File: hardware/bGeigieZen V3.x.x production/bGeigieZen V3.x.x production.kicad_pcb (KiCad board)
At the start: 2 copper layers, 129.4 x 64.6 mm, 16 parts, among them J1 M5 2x15 pin, J10 QI GND, J11 QI charger Plus, J2 Geiger IRover, J3 GPS, J4 Geiger Safepulse, J5 Extra support header, J6 Grove, J8 QI charger ground, J9 QI Plus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

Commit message: Fixed some text on V3.0.5 boards
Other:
- board text added: "Grove"
- board text removed: "Groove"
- board text removed: "bGeigieZen V3.0.4 Production"
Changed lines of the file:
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@@
 		)
 	)
-	(gr_text "bGeigieZen\nV3.0.4  Production"
+	(gr_text "bGeigieZen\nV3.0.5  Production"
 		(at 102.7176 83.006 90)
 		(layer "B.SilkS")
@@
 		)
 	)
-	(gr_text "Groove"
+	(gr_text "Grove"
 		(at 163.83 117.6008 90)
 		(layer "F.SilkS")

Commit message: Updated some traces.
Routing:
- net 3.3V: track 117.2 -> 110.8 mm, vias 0 -> 2
- net /VBATT: track 56.9 -> 54.2 mm
- net /BAT: track 92.8 -> 94.9 mm
- net /RX2: track 39.3 -> 40.5 mm
- net /GIO2 on Core and GIO32 on Core-2: track 101.4 -> 102.1 mm

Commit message: Fixed some traces
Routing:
- net /RX2: track 40.5 -> 39.4 mm
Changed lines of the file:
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@@
-	)
-	(segment
-		(start 126.2822 115.285299)
-		(end 126.2822 117.963)
-		(width 0.25)
-		(layer "B.Cu")
-		(net 2)
 	)
 	(segment
@@
 	)
 	(segment
-		(start 125.9332 118.312)
+		(start 126.2822 116.947)
 		(end 124.9172 118.312)
-		(width 0.25)
-		(layer "B.Cu")
-		(net 2)
-	)
-	(segment
-		(start 126.094 118.312)
-		(end 125.9332 118.312)
 		(width 0.25)
 		(layer "B.Cu")
@@
 	)
 	(segment
-		(start 126.094 117.944)
-		(end 126.094 118.312)
-		(width 0.25)
-		(layer "B.Cu")
-		(net 2)
-	)
-	(segment
-		(start 126.2822 117.963)
-		(end 125.9332 118.312)
+		(start 126.2822 115.285299)
+		(end 126.2822 116.947)
 		(width 0.25)
 		(layer "B.Cu")
@@
 	)
 	(segment
+		(start 135.8244 100.6336)
+		(end 154.2796 100.6336)
+		(width 0.25)
+		(layer "F.Cu")
+		(net 19)
+	)
+	(segment
 		(start 154.2796 100.6336)
-		(end 135.8244 100.6336)
-		(width 0.25)
-		(layer "F.Cu")
-		(net 19)
-	)
-	(segment
-		(start 121.014 116.326)
-		(end 120.205 117.135)
-		(width 0.25)
-		(layer "F.Cu")
-		(net 19)
-	)
-	(segment
-		(start 135.8244 100.6336)
-		(end 121.014 115.444)
-		(width 0.25)
-		(layer "F.Cu")
-		(net 19)
-	)
-	(segment
-		(start 119.837 117.135)
-		(end 119.837 118.0915)
+		(end 158.927985 95.985215)
 		(width 0.25)
 		(layer "F.Cu")
@@
 	)
 	(segment
-		(start 192.8368 93.928)
+		(start 191.981666 95.985215)
 		(end 192.8368 95.130081)
 		(width 0.25)
@@
 	)
 	(segment
-		(start 191.981666 95.985215)
-		(end 158.927985 95.985215)
+		(start 119.8372 118.312)
+		(end 121.014 117.1352)
 		(width 0.25)
 		(layer "F.Cu")
@@
 	)
 	(segment
-		(start 119.837 117.43)
-		(end 119.837 117.724)
+		(start 192.8368 95.130081)
+		(end 192.8368 93.928)
 		(width 0.25)
 		(layer "F.Cu")
@@
 	(segment
 		(start 158.927985 95.985215)
-		(end 154.2796 100.6336)
-		(width 0.25)
-		(layer "F.Cu")
-		(net 19)
-	)
-	(segment
-		(start 192.8368 95.130081)
 		(end 191.981666 95.985215)
+		(width 0.25)
+		(layer "F.Cu")
+		(net 19)
+	)
+	(segment
+		(start 121.014 115.444)
+		(end 135.8244 100.6336)
 		(width 0.25)
 		(layer "F.Cu")
@@
 	)
 	(segment
-		(start 121.014 115.444)
-		(end 121.014 116.326)
-		(width 0.25)
-		(layer "F.Cu")
-		(net 19)
-	)
-	(segment
-		(start 120.205 117.135)
-		(end 119.837 117.135)
+		(start 121.014 117.1352)
+		(end 121.014 115.444)
 		(width 0.25)
 		(layer "F.Cu")
@@
 	)
 	(segment
-		(start 122.3772 118.312)
-		(end 123.554 118.312)
+		(start 151.299 118.542)
+		(end 150.301 119.54)
 		(width 0.25)
 		(layer "B.Cu")
@@
 	)
 	(segment
-		(start 151.299 118.542)
-		(end 154.694 118.542)
+		(start 123.6052 119.54)
+		(end 122.3772 118.312)
+		(width 0.25)
+		(layer "B.Cu")
+		(net 26)
+	)
+	(segment
+		(start 154.694 118.542)
+		(end 151.299 118.542)
 		(width 0.25)
 		(layer "B.Cu")
@@
 	(segment
 		(start 150.301 119.54)
-		(end 151.299 118.542)
+		(end 123.6052 119.54)
 		(width 0.25)
 		(layer "B.Cu")
@@
 	)
 	(segment
-		(start 154.694 118.542)
-		(end 154.6945 118.5415)
-		(width 0.25)
-		(layer "B.Cu")
-		(net 26)
-	)
-	(segment
 		(start 152.985 98.9408)
 		(end 152.985 98.7941)
@@
 	)
 	(segment
-		(start 124.414 119.54)
-		(end 150.301 119.54)
-		(width 0.25)
-		(layer "B.Cu")
-		(net 26)
-	)
-	(segment
-		(start 123.554 118.68)
-		(end 124.414 119.54)
-		(width 0.25)
-		(layer "B.Cu")
-		(net 26)
-	)
-	(segment
-		(start 123.554 118.312)
-		(end 123.554 118.68)
-		(width 0.25)
-		(layer "B.Cu")
+		(start 154.6945 118.5415)
+		(end 154.694 118.542)
+		(width 0.25)
+		(layer "B.Cu")

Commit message: Updated 4.x.x boards and 3.0.3a  with isolated positive battery for filling planes.
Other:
- board text added: "bGeigieZen V3.0.5a Production"
- board text removed: "bGeigieZen V3.0.5 Production"
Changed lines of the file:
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@@
 (kicad_pcb
-	(version 20240225)
+	(version 20240609)
 	(generator "pcbnew")
 	(generator_version "8.99")
@@
 	(paper "A4")
 	(title_block
-		(title "bGeigieZen Production V3.0.5")
-		(date "2024-04-07")
-		(rev "V3.0.5")
+		(title "bGeigieZen Production V3.0.5a")
+		(date "2024-06-16")
+		(rev "V3.0.5a")
 	)
 	(layers
@@
 		(pad_to_mask_clearance 0)
 		(allow_soldermask_bridges_in_footprints no)
+		(tenting front back)
 		(aux_axis_origin 90.4338 71.8155)
 		(grid_origin 124.3076 84.53)
@@
 			(svgprecision 6)
 			(plotframeref no)
-			(viasonmask no)
 			(mode 1)
 			(useauxorigin no)
@@
 		)
 	)
-	(gr_text "bGeigieZen\nV3.0.5  Production"
+	(gr_text "bGeigieZen\nV3.0.5a  Production"
 		(at 102.7176 83.006 90)
 		(layer "B.SilkS")
@@
 		)
 	)
-	(gr_text "bGeigieZen \nV3.0.5\nProduction"
+	(gr_text "bGeigieZen \nV3.0.5a\nProduction"
 		(at 175.8188 122.9856 90)
 		(layer "F.SilkS")
@@
 		(drill 0.4)
 		(layers "F.Cu" "B.Cu")
+		(tenting none)
 		(net 2)
 	)
@@
 		(drill 0.4)
 		(layers "F.Cu" "B.Cu")
+		(tenting none)
 		(net 3)
 	)
@@
 		(drill 0.8)
 		(layers "F.Cu" "B.Cu")
+		(tenting none)
 		(net 4)
 	)
@@
 		(drill 0.8)
 		(layers "F.Cu" "B.Cu")
+		(tenting none)
 		(net 4)
 	)
@@
 		(drill 0.4)
 		(layers "F.Cu" "B.Cu")
+		(tenting none)
 		(net 32)
 	)
@@
 	)
 	(zone
+		(net 0)
+		(net_name "")
+		(layers "F&B.Cu")
+		(hatch full 0.5)
+		(connect_pads
+			(clearance 0)
+		)
+		(min_thickness 0.25)
+		(filled_areas_thickness no)
+		(keepout
+			(tracks allowed)
+			(vias allowed)
+			(pads allowed)
+			(copperpour not_allowed)
+			(footprints allowed)
+		)
+		(fill
+			(thermal_gap 0.5)
+			(thermal_bridge_width 0.5)
+		)
+		(polygon
+			(pts
+				(xy 195.2244 64.718) (xy 215.646 64.718) (xy 216.408 81.228) (xy 195.1736 81.3296)
+			)
+		)
+	)
+	(zone
 		(net 1)
 		(net_name "GND")
@@
 		(polygon
 			(pts
-				(xy 223.3676 60.4) (xy 223.3676 137.87) (xy 79.8576 137.87) (xy 79.8576 60.4)
+				(xy 220.1672 60.4) (xy 220.1672 137.87) (xy 79.8576 137.87) (xy 79.8576 60.4)
 			)
 		)

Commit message: Renamed V3.0.5a boards to V3.0.6 .
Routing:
- net /VBATT: track 54.2 -> 63.7 mm
- net /SCL: track 72.4 -> 77.3 mm
- net 3.3V: track 110.8 -> 115.3 mm
- net /BAT: track 94.9 -> 91.7 mm
- net /SDA: track 55.1 -> 56.0 mm
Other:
- board text added: "bGeigieZen V3.0.6 Production"
- board text removed: "bGeigieZen V3.0.5a Production"
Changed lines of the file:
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@@
 	(paper "A4")
 	(title_block
-		(title "bGeigieZen Production V3.0.5a")
+		(title "bGeigieZen Production V3.0.6")
 		(date "2024-06-16")
-		(rev "V3.0.5a")
+		(rev "V3.0.６")
 	)
 	(layers
@@
 		)
 	)
-	(gr_text "bGeigieZen\nV3.0.5a  Production"
+	(gr_text "bGeigieZen\nV3.0.6  Production"
 		(at 102.7176 83.006 90)
 		(layer "B.SilkS")
@@
 		)
 	)
-	(gr_text "bGeigieZen \nV3.0.5a\nProduction"
+	(gr_text "bGeigieZen \nV3.0.6\nProduction"
 		(at 175.8188 122.9856 90)
 		(layer "F.SilkS")
@@
 	)
 	(segment
+		(start 150.935 116.5422)
+		(end 154.6945 116.5422)
+		(width 0.5)
+		(layer "F.Cu")
+		(net 4)
+	)
+	(segment
+		(start 150.314906 113.1172)
+		(end 150.314906 115.922106)
+		(width 0.5)
+		(layer "F.Cu")
+		(net 4)
+	)
+	(segment
+		(start 150.314906 103.175894)
+		(end 151.6888 101.802)
+		(width 0.5)
+		(layer "F.Cu")
+		(net 4)
+	)
+	(segment
 		(start 129.9972 115.772)
 		(end 132.652 113.1172)
@@
 	)
 	(segment
+		(start 151.6888 101.802)
+		(end 156.860066 101.802)
+		(width 0.5)
+		(layer "F.Cu")
+		(net 4)
+	)
+	(segment
 		(start 129.9972 115.772)
 		(end 129.997 115.772)
@@
 	)
 	(segment
-		(start 160.5788 94.5884)
-		(end 161.100615 95.110215)
-		(width 0.5)
-		(layer "F.Cu")
-		(net 4)
-	)
-	(segment
-		(start 160.009509 98.371591)
+		(start 156.860066 101.802)
 		(end 160.290475 98.371591)
 		(width 0.5)
@@
 	)
 	(segment
-		(start 150.314906 108.066194)
-		(end 160.009509 98.371591)
+		(start 160.5788 94.5884)
+		(end 161.100615 95.110215)
 		(width 0.5)
 		(layer "F.Cu")
@@
 	(segment
 		(start 150.314906 113.1172)
-		(end 150.314906 108.066194)
+		(end 150.314906 103.175894)
 		(width 0.5)
 		(layer "F.Cu")
@@
 	)
 	(segment
-		(start 150.314906 113.1172)
-		(end 153.739906 116.5422)
-		(width 0.5)
-		(layer "F.Cu")
-		(net 4)
-	)
-	(segment
 		(start 188.7224 92.3024)
 		(end 193.7512 92.3024)
@@
 	)
 	(segment
-		(start 153.739906 116.5422)
-		(end 154.6945 116.5422)
+		(start 132.652 113.1172)
+		(end 150.314906 113.1172)
 		(width 0.5)
 		(layer "F.Cu")
@@
 	)
 	(segment
-		(start 132.652 113.1172)
-		(end 150.314906 113.1172)
+		(start 150.314906 115.922106)
+		(end 150.935 116.5422)
 		(width 0.5)
 		(layer "F.Cu")
@@
 	)
 	(segment
-		(start 186.588 98.8301)
-		(end 183.534 101.884)
-		(width 0.5)
-		(layer "B.Cu")
-		(net 7)
-	)
-	(segment
 		(start 186.6302 75.963)
 		(end 186.588 75.9208)
@@
 	)
 	(segment
+		(start 175.7172 86.7916)
+		(end 175.7172 99.1604)
+		(width 0.5)
+		(layer "B.Cu")
+		(net 7)
+	)
+	(segment
 		(start 203.339 73.8688)
 		(end 196.6908 73.8688)
@@
 	)
 	(segment
-		(start 186.588 75.9208)
-		(end 186.588 98.8301)
-		(width 0.5)
-		(layer "B.Cu")
-		(net 7)
-	)
-	(segment
 		(start 184.506 73.838)
 		(end 186.588 75.9208)
@@
 	)
 	(segment
-		(start 183.534 101.884)
+		(start 184.506 73.8383)
+		(end 184.506 73.8381)
+		(width 0.25)
+		(layer "B.Cu")
+		(net 7)
+	)
+	(segment
+		(start 178.4413 101.8845)
 		(end 183.534 101.8845)
 		(width 0.5)
@@
 	)
 	(segment
-		(start 184.506 73.8383)
-		(end 184.506 73.8381)
-		(width 0.25)
+		(start 186.588 75.9208)
+		(end 175.7172 86.7916)
+		(width 0.5)
 		(layer "B.Cu")
 		(net 7)
@@
 	)
 	(segment
+		(start 175.7172 99.1604)
+		(end 178.4413 101.8845)
+		(width 0.5)
+		(layer "B.Cu")
+		(net 7)
+	)
+	(segment
 		(start 135.8244 100.6336)
 		(end 154.2796 100.6336)
@@
 	)
 	(segment
-		(start 152.985 99.6767)
-		(end 152.985 98.9412)
+		(start 149.1488 116.3918)
+		(end 149.1488 102.5567)
 		(width 0.25)
 		(layer "B.Cu")
@@
 	)
 	(segment
+		(start 151.299 118.542)
+		(end 149.1488 116.3918)
+		(width 0.25)
+		(layer "B.Cu")
+		(net 26)
+	)
+	(segment
 		(start 154.694 118.542)
 		(end 151.299 118.542)
@@
 	)
 	(segment
-		(start 152.985 98.9408)
-		(end 152.985 98.7941)
-		(width 0.25)
-		(layer "B.Cu")
-		(net 26)
-	)
-	(segment
-		(start 152.985 98.7941)
-		(end 152.985 98.7205)
-		(width 0.25)
-		(layer "B.Cu")
-		(net 26)
-	)
-	(segment
 		(start 154.6945 118.5415)
 		(end 154.6945 118.5422)
@@
 	)
 	(segment
-		(start 152.985 98.9412)
-		(end 152.985 98.9408)
+		(start 149.1488 102.5567)
+		(end 152.985 98.7205)
 		(width 0.25)
 		(layer "B.Cu")
@@
 	)
 	(segment
-		(start 155.751 117.485)
-		(end 155.751 102.443)
-		(width 0.25)
-		(layer "B.Cu")
-		(net 26)
-	)
-	(segment
-		(start 155.751 102.443)
-		(end 152.985 99.6767)
-		(width 0.25)
-		(layer "B.Cu")
-		(net 26)
-	)
-	(segment
-		(start 154.6945 118.5415)
-		(end 155.751 117.485)
-		(width 0.25)
-		(layer "B.Cu")
-		(net 26)
-	)
-	(segment
 		(start 154.6945 118.5415)
 		(end 154.694 118.542)
@@
 	)
 	(segment
-		(start 156.208 119.028)
-		(end 156.208 89.0237)
+		(start 154.4596 99.375)
+		(end 154.4596 87.2747)
+		(width 0.25)
+		(layer "B.Cu")
+		(net 27)
+	)
+	(segment
+		(start 151.8412 113.3336)
+		(end 150.876 112.3684)
+		(width 0.25)
+		(layer "B.Cu")
+		(net 27)
+	)
+	(segment
+		(start 155.9945 119.2415)
+		(end 155.9945 114.003722)
 		(width 0.25)
 		(layer "B.Cu")
@@
 	)
 	(segment
+		(start 155.9945 114.003722)
+		(end 155.232978 113.2422)
+		(width 0.25)
+		(layer "B.Cu")
+		(net 27)
+	)
+	(segment
+		(start 154.156022 113.2422)
+		(end 154.064622 113.3336)
+		(width 0.25)
+		(layer "B.Cu")
+		(net 27)
+	)
+	(segment
+		(start 150.876 112.3684)
+		(end 150.876 102.9586)
+		(width 0.25)
+		(layer "B.Cu")
+		(net 27)
+	)
+	(segment
+		(start 150.876 102.9586)
+		(end 154.4596 99.375)
+		(width 0.25)
+		(layer "B.Cu")
+		(net 27)
+	)
+	(segment
+		(start 155.232978 113.2422)
+		(end 154.156022 113.2422)
+		(width 0.25)
+		(layer "B.Cu")
+		(net 27)
+	)
+	(segment
 		(start 154.694 120.542)
 		(end 154.6942 120.5418)
@@
 	)
 	(segment
+		(start 154.064622 113.3336)
+		(end 151.8412 113.3336)
+		(width 0.25)
+		(layer "B.Cu")
+		(net 27)
+	)
+	(segment
 		(start 154.6942 120.5418)
-		(end 156.208 119.028)
+		(end 155.9945 119.2415)
 		(width 0.25)
 		(layer "B.Cu")
@@
 	)
 	(segment
-		(start 156.208 89.0237)
+		(start 154.4596 87.2747)
 		(end 153.6299 86.445)
 		(width 0.25)
@@
 	)
 	(segment
-		(start 151.9936 83.5648)
-		(end 150.2156 85.3428)
-		(width 0.5)
-		(layer "B.Cu")
-		(net 30)
-	)
-	(segment
-		(start 150.2156 85.3428)
-		(end 150.2156 88.0864)
+		(start 181.506 73.838)
+		(end 171.7792 83.5648)
 		(width 0.5)
 		(layer "B.Cu")
@@
 	)
 	(segment
-		(start 181.506 76.506)
-		(end 174.4472 83.5648)
-		(width 0.5)
-		(layer "B.Cu")
-		(net 30)
-	)
-	(segment
-		(start 108.737 114.172)
-		(end 107.1372 115.7718)
-		(width 0.5)
-		(layer "B.Cu")
-		(net 30)
-	)
-	(segment
 		(start 107.1372 115.7718)
 		(end 107.1372 115.772)
@@
 	)
 	(segment
-		(start 124.13 114.172)
-		(end 108.737 114.172)
+		(start 139.3442 83.5648)
+		(end 107.1372 115.7718)
 		(width 0.5)
 		(layer "B.Cu")
@@
 	)
 	(segment
-		(start 174.4472 83.5648)
-		(end 151.9936 83.5648)
+		(start 171.7792 83.5648)
+		(end 139.3442 83.5648)
 		(width 0.5)
 		(layer "B.Cu")
@@
 	)
 	(segment
-		(start 150.2156 88.0864)
-		(end 124.13 114.172)
-		(width 0.5)
-		(layer "B.Cu")
-		(net 30)
-	)
-	(segment
 		(start 181.506 73.838)
 		(end 181.506 73.8382)
@@
 		(layer "B.Cu")
 		(net 30)
-	)
-	(segment
-		(start 181.506 73.838)
-		(end 181.506 76.506)
-		(width 0.5)
-		(layer "B.Cu")
-		(net 30)

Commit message: Updated 3.0.6 board
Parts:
- moved SW1 46.8 mm to (184.7, 120.6)
- moved J4 7.13 mm to (190.8, 86.8)
- moved J5 7.13 mm to (160.9, 103.3)
- moved J3 3.35 mm to (153.7, 101.8)
- moved BT1 1.80 mm to (176.3, 75.7)
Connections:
- BT1 pad GND@2: (no net) -> Net-(BT1--)
- BT1 pad GND@3: (no net) -> Net-(BT1--)
- BT1 pad PWR@2: (no net) -> /VBATT
- BT1 pad PWR@3: (no net) -> /VBATT
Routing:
- net /GIO2 on Core and GIO32 on Core-2: track 101.8 -> 126.1 mm
- net 3.3V: track 115.3 -> 132.4 mm, vias 2 -> 0
- net /BAT: track 91.7 -> 107.7 mm
- net /SCL: track 77.3 -> 68.8 mm
- net Net-(BT1--): track 50.5 -> 58.4 mm
- net /VBATT: track 63.7 -> 67.7 mm
- net /SDA: track 56.0 -> 55.0 mm
- net /TX2: track 38.9 -> 39.6 mm, vias 1 -> 0
- net /RX2: track 39.4 -> 39.3 mm, vias 1 -> 0
- net GND: vias 0 -> 1
- net (no net): vias 0 -> 1

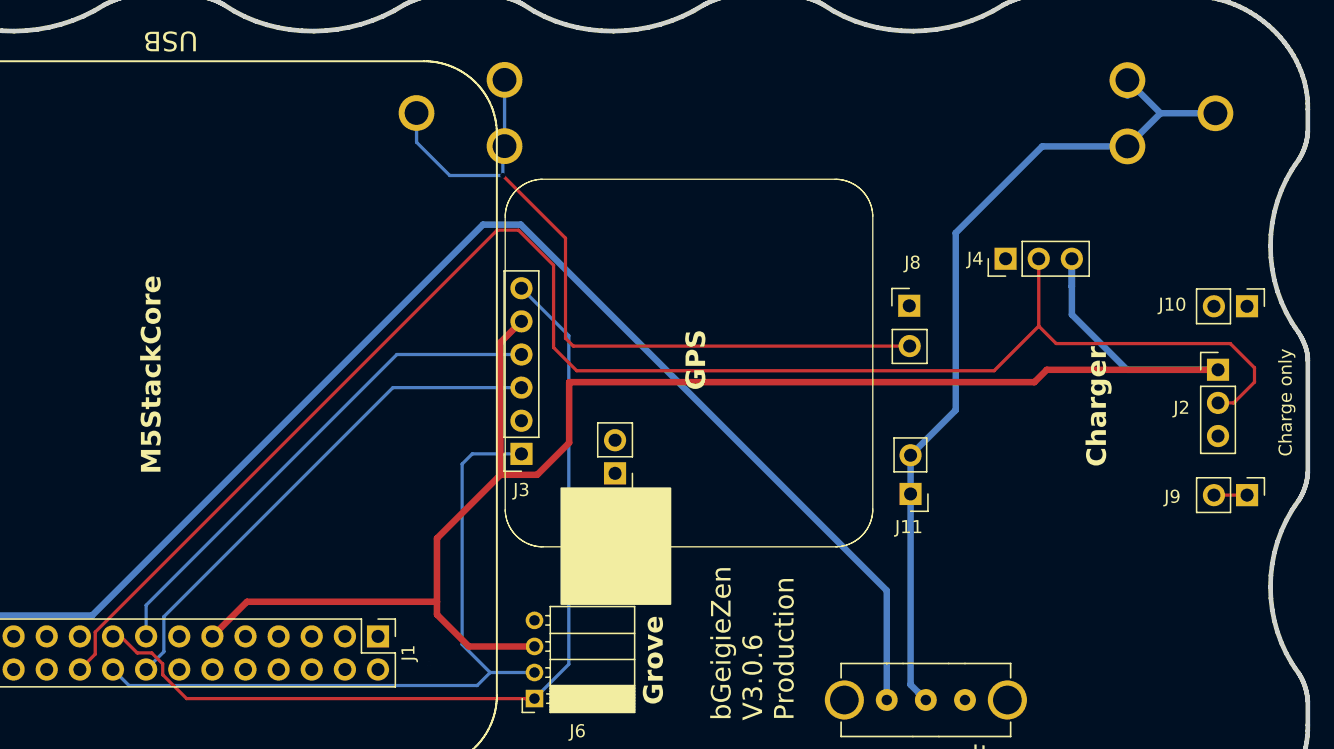
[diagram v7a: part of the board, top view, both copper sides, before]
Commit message: remove Irover pins. The Irover fits now at the same location as the safeppulse.
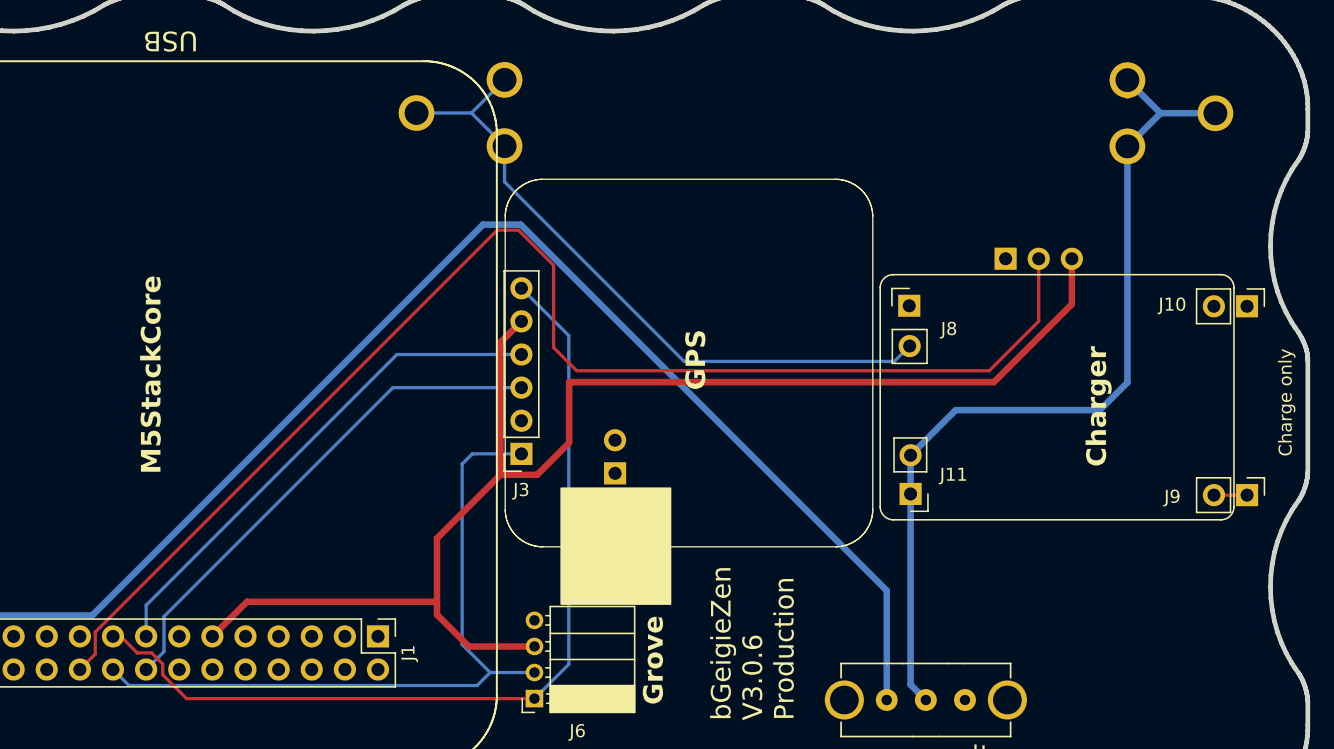
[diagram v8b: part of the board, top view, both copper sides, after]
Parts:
- removed J2: Geiger IRover, Connector_PinHeader_2.54mm:PinHeader_1x03_P2.54mm_Vertical
- added REF**: LOGO, bGeigieZen:18650 map, B.Cu at (175.9, 76.2)
- BT1: value 3.7 V Lipo -> 3.7 V Lipo; footprint bGeigieRaku_M5_1015:BATTERY_18650-HOLDER -> bGeigieZen:BATTERY_18650-HOLDER
- H4, H6: footprint MountingHole:MountingHole_3.2mm_M3 -> bGeigieZen:MountingHole_3.2mm_M3
- J1: footprint Connector_PinHeader_2.54mm:PinHeader_2x15_P2.54mm_Vertical -> bGeigieZen:PinHeader_2x15_P2.54mm_Vertical
- J10, J5, J8, J9: footprint Connector_PinHeader_2.54mm:PinHeader_1x02_P2.54mm_Vertical -> bGeigieZen:PinHeader_1x02_P2.54mm_Vertical
- J3: footprint Connector_PinSocket_2.54mm:PinSocket_1x06_P2.54mm_Vertical -> bGeigieZen:PinSocket_1x06_P2.54mm_Vertical
- J4: footprint Connector_PinHeader_2.54mm:PinHeader_1x03_P2.54mm_Vertical -> bGeigieZen:PinHeader_1x03_P2.54mm_Vertical
- J6: footprint Connector_PinSocket_2.00mm:PinSocket_1x04_P2.00mm_Horizontal -> bGeigieZen:PinSocket_1x04_P2.00mm_Horizontal
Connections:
- BT1 pad GND@2: Net-(BT1--) -> (no net)
- BT1 pad GND@3: Net-(BT1--) -> (no net)
- BT1 pad PWR@2: /VBATT -> (no net)
- BT1 pad PWR@3: /VBATT -> (no net)
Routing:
- net 3.3V: track 132.4 -> 107.4 mm
- net /GIO2 on Core and GIO32 on Core-2: track 126.1 -> 103.4 mm
- net Net-(BT1--): track 58.4 -> 51.6 mm, vias 1 -> 0
- net /VBATT: track 67.7 -> 70.3 mm
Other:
- board text removed: "IRover pins"
- board text removed: "screws for the display are M3 12mm"
